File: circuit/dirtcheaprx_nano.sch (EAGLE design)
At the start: 23 parts, among them IC1 MCP1703T-3302E/CB

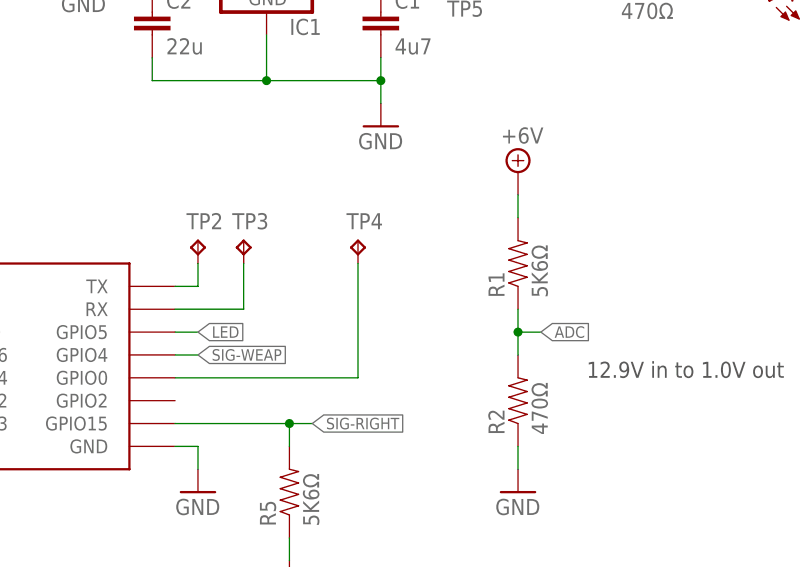
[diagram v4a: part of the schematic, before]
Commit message: resistor on GPIO0, flipped weap servo connector
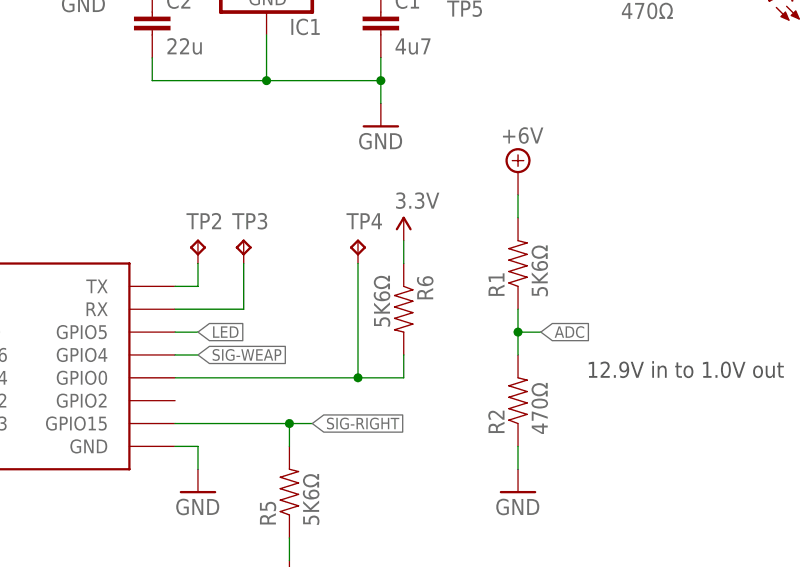
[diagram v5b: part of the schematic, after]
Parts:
- added R6: 5K6Ω, dirtcheaprx_nano:RESISTOR0603-RES
- SERVO1: value SERVO-SMD-EDGE-1 -> SERVO-SMD-EDGE-1F; device dirtcheaprx_nano:SERVO-SMD-EDGE-1 -> dirtcheaprx_nano:SERVO-SMD-EDGE-1F
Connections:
- net 3.3V: now also R6.1
- net N$11: now also R6.2
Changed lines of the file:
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@@
 <layer number="16" name="Bottom" color="1" fill="1" visible="yes" active="no"/>
 <layer number="17" name="Pads" color="2" fill="1" visible="yes" active="no"/>
-<layer number="18" name="Vias" color="2" fill="1" visible="yes" active="no"/>
+<layer number="18" name="Vias" color="14" fill="1" visible="yes" active="no"/>
 <layer number="19" name="Unrouted" color="6" fill="1" visible="yes" active="no"/>
 <layer number="20" name="Dimension" color="15" fill="1" visible="yes" active="no"/>
@@
 <part name="BAT1" library="dirtcheaprx_nano" deviceset="BATTERY" device="-WIRE-CONN"/>
 <part name="SUPPLY1" library="dirtcheaprx_nano" deviceset="+6V" device=""/>
-<part name="SERVO1" library="dirtcheaprx_nano" deviceset="SERVO" device="-SMD-EDGE-1" value="SERVO-SMD-EDGE-1"/>
+<part name="SERVO1" library="dirtcheaprx_nano" deviceset="SERVO" device="-SMD-EDGE-1F" value="SERVO-SMD-EDGE-1F"/>
 <part name="SERVO2" library="dirtcheaprx_nano" deviceset="SERVO" device="-SMD-EDGE-1" value="SERVO-SMD-EDGE-1"/>
 <part name="SERVO3" library="dirtcheaprx_nano" deviceset="SERVO" device="-SMD-EDGE-1" value="SERVO-SMD-EDGE-1"/>
@@
 <part name="R5" library="dirtcheaprx_nano" deviceset="RESISTOR" device="0603-RES" value="5K6Ω"/>
 <part name="GND10" library="dirtcheaprx_nano" deviceset="GND" device=""/>
+<part name="R6" library="dirtcheaprx_nano" deviceset="RESISTOR" device="0603-RES" value="5K6Ω"/>
+<part name="P+5" library="dirtcheaprx_nano" deviceset="3.3V" device=""/>
 </parts>
 <sheets>
@@
 <instance part="R5" gate="G$1" x="33.02" y="-25.4" rot="R90"/>
 <instance part="GND10" gate="1" x="33.02" y="-35.56"/>
+<instance part="R6" gate="G$1" x="45.72" y="-5.08" rot="R270"/>
+<instance part="P+5" gate="G$1" x="45.72" y="2.54"/>
 </instances>
 <busses>
@@
 <wire x1="-27.94" y1="20.32" x2="-30.48" y2="20.32" width="0.1524" layer="91"/>
 <wire x1="-30.48" y1="20.32" x2="-30.48" y2="22.86" width="0.1524" layer="91"/>
+</segment>
+<segment>
+<pinref part="R6" gate="G$1" pin="1"/>
+<pinref part="P+5" gate="G$1" pin="3.3V"/>
+<wire x1="45.72" y1="0" x2="45.72" y2="2.54" width="0.1524" layer="91"/>
 </segment>
 </net>
@@
 <wire x1="20.32" y1="-12.7" x2="40.64" y2="-12.7" width="0.1524" layer="91"/>
 <wire x1="40.64" y1="-12.7" x2="40.64" y2="0" width="0.1524" layer="91"/>
-</segment>
-</net>
+<pinref part="R6" gate="G$1" pin="2"/>
+<wire x1="40.64" y1="-12.7" x2="45.72" y2="-12.7" width="0.1524" layer="91"/>
+<wire x1="45.72" y1="-12.7" x2="45.72" y2="-10.16" width="0.1524" layer="91"/>
+<junction x="40.64" y="-12.7"/>
+</segment>
+</net>
